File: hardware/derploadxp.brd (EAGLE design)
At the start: 59.1 x 61 mm, 53 parts, among them IC3 TC7660SO-08, J1 AVR_SPI_PRG_6NS, J2 POWER_JACKPTH, U1 ATMEGA328P_PDIP

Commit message: Resolved Issue #1 and #2 moved items around to add project name and version to top layer silkscreen
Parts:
- moved Y1 7.67 mm to (40.0, 32.4)
- moved C13 5.75 mm to (50.2, 36.8), turned to 270 degrees
- moved C14 5.68 mm to (45.7, 37.5)
- moved C1 4.58 mm to (48.3, 36.8), turned to 270 degrees
- moved C12 3.17 mm to (34.3, 36.8)
- moved C15 3.17 mm to (39.4, 36.8)
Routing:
- net PB7: track 22.8 -> 13.1 mm
- net PB6: track 17.4 -> 7.73 mm
- net 5V: track 155.4 -> 164.1 mm
- net N$11: track 27.2 -> 20.0 mm
- net GND: track 134.9 -> 133.0 mm
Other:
- board text added: "Derpload"
- board text added: "v1.0.0"

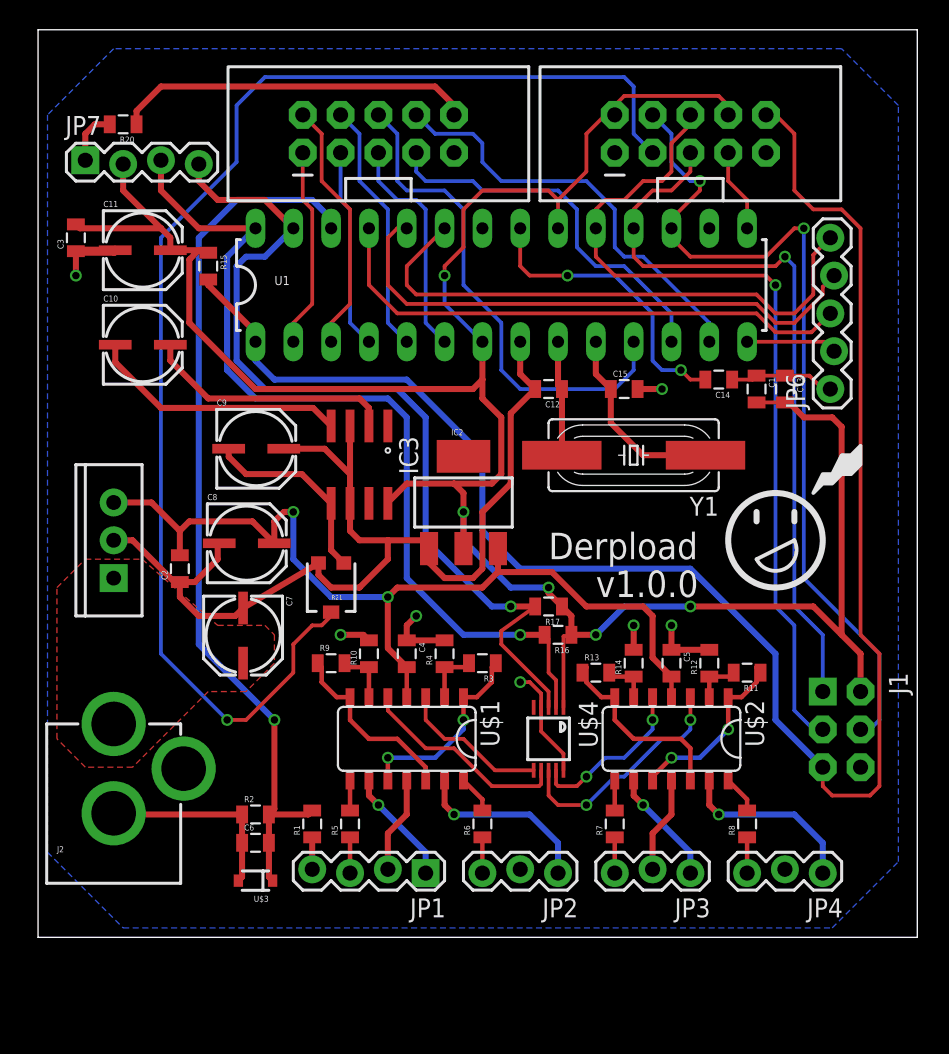
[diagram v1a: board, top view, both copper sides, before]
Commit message: Added one of two mounting holes to resolve Issue #3
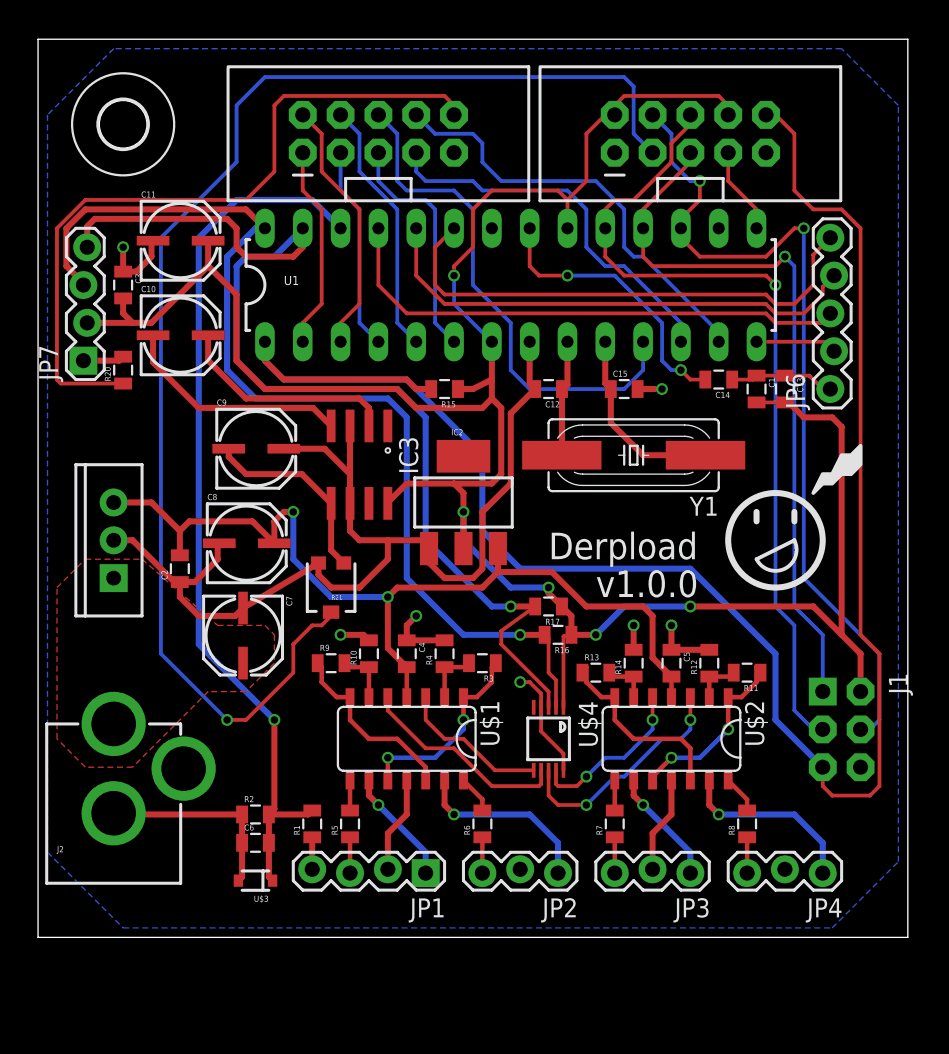
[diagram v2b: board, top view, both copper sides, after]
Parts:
- added U$7: (no value), holes:3,2
- moved R15 17.9 mm to (27.3, 36.8), turned to 180 degrees
- moved R20 16.5 mm to (5.71, 38.1), turned to 90 degrees
- moved JP7 13.3 mm to (3.17, 38.7), turned to 90 degrees
- moved C3 4.49 mm to (5.71, 43.8), turned to 270 degrees
- moved C11 2.62 mm to (9.53, 47.0)
- moved C10 2.62 mm to (9.53, 40.6)
- moved U1 0.64 mm to (31.8, 43.8)
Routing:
- net LED-: track 24.1 -> 48.6 mm
- net SDA: track 61.0 -> 72.2 mm
- net SCL: track 60.0 -> 69.8 mm
- net RESET: track 117.1 -> 124.2 mm
- net ROTARYA: track 37.3 -> 33.6 mm
- net ROTARYB: track 37.8 -> 34.4 mm
- net N$4: track 17.4 -> 15.5 mm
- net N$2: track 16.9 -> 15.0 mm
- net CS2: track 58.0 -> 56.4 mm
- net CS1: track 50.3 -> 48.6 mm
- net 5V: track 164.1 -> 162.7 mm
- net SELECT: track 36.6 -> 35.5 mm
- net N$11: track 20.0 -> 19.0 mm
- net A0: track 57.6 -> 56.7 mm
- net DB4: track 15.3 -> 15.9 mm
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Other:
- board size 59.1 x 61 mm -> 58.4 x 60.3 mm

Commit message: Added two of two mounting holes to resolve Issue #3
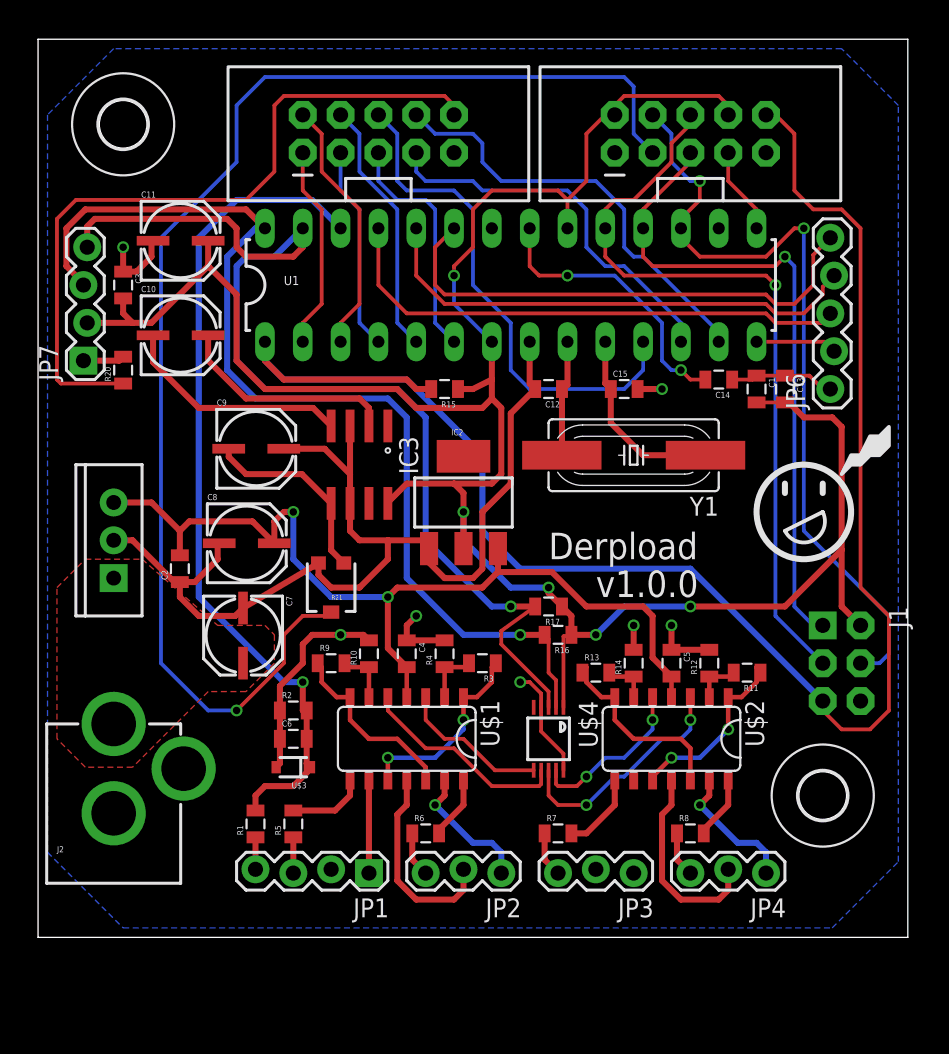
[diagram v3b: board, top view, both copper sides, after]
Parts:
- added U$5: (no value), holes:3,2
- moved U$3 8.03 mm to (17.1, 11.4)
- moved C6 7.43 mm to (17.1, 13.3)
- moved R2 7.43 mm to (17.1, 15.2)
- moved J1 4.44 mm to (54.0, 18.4)
- moved R7 3.86 mm to (34.9, 6.99), turned to 0 degrees
- moved R8 3.86 mm to (43.8, 6.99), turned to 0 degrees
- moved R6 3.86 mm to (26.0, 6.99), turned to 0 degrees
- moved JP1 3.81 mm to (22.2, 4.45)
- moved JP2 3.81 mm to (31.1, 4.45)
- moved R1 3.81 mm to (14.6, 7.62)
- moved R5 3.81 mm to (17.1, 7.62)
- moved JP3 3.81 mm to (40.0, 4.45)
- moved JP4 3.81 mm to (48.9, 4.45)
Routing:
- net GND: track 132.6 -> 145.5 mm
- net RESET: track 124.2 -> 115.4 mm
- net VSHUNT3: track 7.80 -> 0.00 mm, vias 1 -> 0
- net CS2: track 56.4 -> 51.6 mm
- net CS1: track 48.6 -> 44.5 mm
- net 5V: track 162.7 -> 159.0 mm
- net A0: track 56.7 -> 53.1 mm
- net N$10: track 2.02 -> 5.34 mm
- net VSENSE: track 59.9 -> 56.6 mm
- net VSHUNT2: track 12.3 -> 9.07 mm
- net VSHUNT4: track 12.3 -> 9.07 mm
- net N$3: track 2.02 -> 5.24 mm
- net N$8: track 2.54 -> 4.23 mm
- net N$9: track 2.54 -> 4.23 mm
- net VSHUNT1: track 7.80 -> 6.22 mm, vias 1 -> 0
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
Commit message: Added 12V aux port
Addresses issue #11
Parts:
- added JP5: (no value), SparkFun-Connectors:1X02_LOCK
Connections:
- net 12V: now also JP5.2
- net GND: now also JP5.1
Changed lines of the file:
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@@
 <?xml version="1.0" encoding="utf-8"?>
 <!DOCTYPE eagle SYSTEM "eagle.dtd">
-<eagle version="6.4">
+<eagle version="6.3">
 <drawing>
 <settings>
@@
 <layers>
 <layer number="1" name="Top" color="4" fill="1" visible="yes" active="yes"/>
+<layer number="2" name="Route2" color="1" fill="3" visible="no" active="no"/>
+<layer number="3" name="Route3" color="4" fill="3" visible="no" active="no"/>
+<layer number="4" name="Route4" color="1" fill="4" visible="no" active="no"/>
+<layer number="5" name="Route5" color="4" fill="4" visible="no" active="no"/>
+<layer number="6" name="Route6" color="1" fill="8" visible="no" active="no"/>
+<layer number="7" name="Route7" color="4" fill="8" visible="no" active="no"/>
+<layer number="8" name="Route8" color="1" fill="2" visible="no" active="no"/>
+<layer number="9" name="Route9" color="4" fill="2" visible="no" active="no"/>
+<layer number="10" name="Route10" color="1" fill="7" visible="no" active="no"/>
+<layer number="11" name="Route11" color="4" fill="7" visible="no" active="no"/>
+<layer number="12" name="Route12" color="1" fill="5" visible="no" active="no"/>
+<layer number="13" name="Route13" color="4" fill="5" visible="no" active="no"/>
+<layer number="14" name="Route14" color="1" fill="6" visible="no" active="no"/>
+<layer number="15" name="Route15" color="4" fill="6" visible="no" active="no"/>
 <layer number="16" name="Bottom" color="1" fill="1" visible="yes" active="yes"/>
 <layer number="17" name="Pads" color="2" fill="1" visible="yes" active="yes"/>
@@
 <element name="U$7" library="holes" package="3,2" value="" x="5.715" y="54.61"/>
 <element name="U$5" library="holes" package="3,2" value="" x="52.705" y="9.525"/>
+<element name="JP5" library="SparkFun-Connectors" package="1X02_LOCK" value="" x="1.905" y="-4.445"/>
 </elements>
 <signals>
@@
 <wire x1="17.78" y1="19.685" x2="18.415" y2="20.32" width="0.4064" layer="1"/>
 <wire x1="18.415" y1="20.32" x2="20.32" y2="20.32" width="0.4064" layer="1"/>
+<contactref element="JP5" pad="1"/>
+<wire x1="30.48" y1="47.625" x2="38.735" y2="52.705" width="0" layer="19" extent="1-1"/>
+<wire x1="33.02" y1="40.005" x2="30.48" y2="47.625" width="0" layer="19" extent="1-1"/>
+<wire x1="25.4" y1="21.59" x2="27.305" y2="24.13" width="0" layer="19" extent="1-1"/>
+<wire x1="22.225" y1="19.95" x2="24.765" y2="19.95" width="0" layer="19" extent="1-1"/>
+<wire x1="32.385" y1="17.145" x2="27.305" y2="19.95" width="0" layer="19" extent="1-1"/>
+<wire x1="40.27" y1="36.83" x2="33.39" y2="36.83" width="0" layer="19" extent="1-1"/>
+<wire x1="46.62" y1="37.465" x2="41.91" y2="36.83" width="0" layer="19" extent="1-1"/>
+<wire x1="40.005" y1="19.315" x2="33.79" y2="16.375" width="0" layer="19" extent="1-1"/>
+<wire x1="42.545" y1="20.955" x2="40.005" y2="20.955" width="0" layer="19" extent="1-1"/>
+<wire x1="37.465" y1="4.572" x2="35.29" y2="11.2219" width="0" layer="19" extent="1-1"/>
+<wire x1="41.91" y1="3.81" x2="37.465" y2="4.572" width="0" layer="19" extent="1-1"/>
+<wire x1="19.685" y1="4.572" x2="15.995" y2="11.43" width="0" layer="19" extent="1-1"/>
+<wire x1="24.13" y1="3.81" x2="19.685" y2="4.572" width="0" layer="19" extent="1-1"/>
+<wire x1="55.245" y1="15.875" x2="45.085" y2="19.315" width="0" layer="19" extent="1-1"/>
+<wire x1="5.08" y1="8.335" x2="15.995" y2="11.43" width="0" layer="19" extent="1-1"/>
+<wire x1="5.45" y1="38.735" x2="5.08" y2="26.67" width="0" layer="19" extent="1-1"/>
+<wire x1="5.715" y1="44.715" x2="5.715" y2="39" width="0" layer="19" extent="1-1"/>
+<wire x1="1.7272" y1="-4.445" x2="5.08" y2="8.335" width="0" layer="19" extent="1-1"/>
 </signal>
 <signal name="VSENSE">
@@
 <wire x1="10.16" y1="27.94" x2="14.4" y2="27.94" width="0.4064" layer="1"/>
 <wire x1="14.4" y1="27.94" x2="15.87" y2="26.47" width="0.4064" layer="1"/>
+<contactref element="JP5" pad="2"/>
+<wire x1="4.6228" y1="-4.445" x2="24.765" y2="16.135" width="0" layer="19" extent="1-1"/>
 </signal>
 <signal name="N$5">

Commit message: Added PDF and placed fan port on Board
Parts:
- moved JP5 38.8 mm to (3.81, 34.3)
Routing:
- net 12V: track 62.2 -> 67.9 mm
- net GND: track 145.5 -> 150.9 mm
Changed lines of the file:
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@@
 <element name="U$7" library="holes" package="3,2" value="" x="5.715" y="54.61"/>
 <element name="U$5" library="holes" package="3,2" value="" x="52.705" y="9.525"/>
-<element name="JP5" library="SparkFun-Connectors" package="1X02_LOCK" value="" x="1.905" y="-4.445"/>
+<element name="JP5" library="SparkFun-Connectors" package="1X02_LOCK" value="" x="3.81" y="34.29"/>
 </elements>
 <signals>
@@
 <wire x1="7.62" y1="45.72" x2="7.62" y2="46.685" width="0.4064" layer="1"/>
 <wire x1="7.62" y1="46.685" x2="7.725" y2="46.79" width="0.4064" layer="1"/>
-<wire x1="3.048" y1="38.735" x2="5.45" y2="38.735" width="0.4064" layer="1"/>
-<wire x1="5.45" y1="38.735" x2="5.715" y2="39" width="0.4064" layer="1"/>
 <via x="5.715" y="46.355" extent="1-16" drill="0.5"/>
 <wire x1="5.715" y1="44.715" x2="5.715" y2="46.355" width="0.4064" layer="1"/>
@@
 <wire x1="37.465" y1="4.572" x2="35.29" y2="11.2219" width="0" layer="19" extent="1-1"/>
 <wire x1="41.91" y1="3.81" x2="37.465" y2="4.572" width="0" layer="19" extent="1-1"/>
+<wire x1="3.048" y1="38.735" x2="3.6322" y2="34.29" width="0" layer="19" extent="1-1"/>
+<wire x1="5.715" y1="39" x2="3.048" y2="38.735" width="0" layer="19" extent="1-1"/>
+<wire x1="5.715" y1="44.715" x2="5.715" y2="39" width="0" layer="19" extent="1-1"/>
 <wire x1="19.685" y1="4.572" x2="15.995" y2="11.43" width="0" layer="19" extent="1-1"/>
 <wire x1="24.13" y1="3.81" x2="19.685" y2="4.572" width="0" layer="19" extent="1-1"/>
 <wire x1="55.245" y1="15.875" x2="45.085" y2="19.315" width="0" layer="19" extent="1-1"/>
 <wire x1="5.08" y1="8.335" x2="15.995" y2="11.43" width="0" layer="19" extent="1-1"/>
-<wire x1="5.45" y1="38.735" x2="5.08" y2="26.67" width="0" layer="19" extent="1-1"/>
-<wire x1="5.715" y1="44.715" x2="5.715" y2="39" width="0" layer="19" extent="1-1"/>
-<wire x1="1.7272" y1="-4.445" x2="5.08" y2="8.335" width="0" layer="19" extent="1-1"/>
+<wire x1="3.6322" y1="34.29" x2="3.6322" y2="28.1178" width="0.4064" layer="16"/>
+<wire x1="3.6322" y1="28.1178" x2="5.08" y2="26.67" width="0.4064" layer="16"/>
 </signal>
 <signal name="VSENSE">
@@
 <wire x1="14.4" y1="27.94" x2="15.87" y2="26.47" width="0.4064" layer="1"/>
 <contactref element="JP5" pad="2"/>
-<wire x1="4.6228" y1="-4.445" x2="24.765" y2="16.135" width="0" layer="19" extent="1-1"/>
+<wire x1="6.5278" y1="34.29" x2="6.5278" y2="30.6578" width="0.4064" layer="16"/>
+<wire x1="6.5278" y1="30.6578" x2="5.08" y2="29.21" width="0.4064" layer="16"/>
 </signal>
 <signal name="N$5">

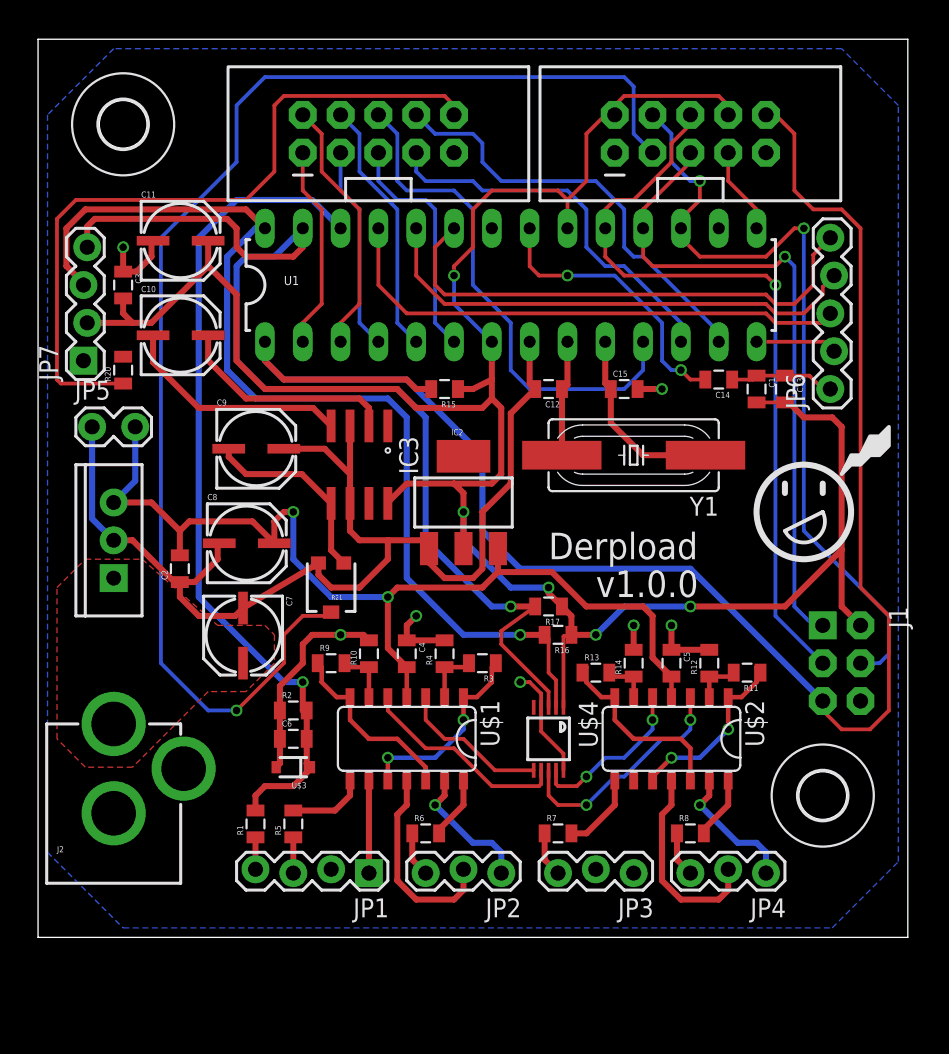
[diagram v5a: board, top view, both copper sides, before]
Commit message: rearranged and corrected visible silkscreen for component values and names to solve Issue #8
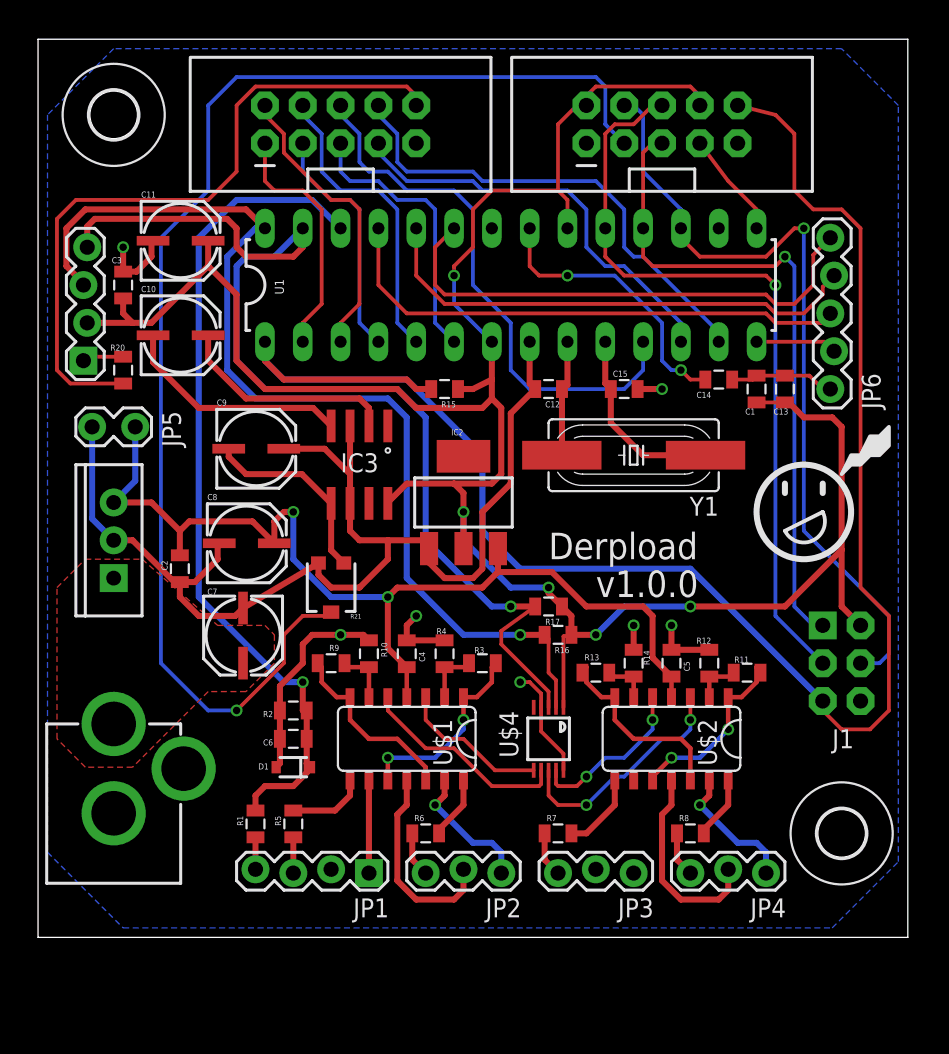
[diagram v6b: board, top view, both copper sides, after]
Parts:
- J1: value AVR_SPI_PRG_6NS -> SPI
- moved U$5 2.84 mm to (54.0, 6.99)
- moved LCD2 2.62 mm to (20.3, 54.6)
- moved LCD1 2.01 mm to (41.9, 54.6)
- moved U$7 0.90 mm to (5.08, 55.2)
- renumbered U$3 to D1
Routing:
- net DB7: track 29.2 -> 32.8 mm
- net DB3: track 17.3 -> 20.5 mm
- net DB0: track 13.8 -> 16.6 mm
- net DB4: track 15.9 -> 18.7 mm
- net GND: track 150.9 -> 153.7 mm
- net LED-: track 48.9 -> 46.3 mm
- net DB6: track 26.0 -> 28.4 mm
- net DB1: track 17.3 -> 19.8 mm
- net DB2: track 13.8 -> 16.2 mm
- net DB5: track 34.5 -> 37.0 mm
- net RESET: track 115.4 -> 117.4 mm
- net VO: track 89.0 -> 87.6 mm
- net CLK: track 5.87 -> 7.14 mm
- net 5V: track 159.0 -> 158.5 mm
- net A0: track 53.1 -> 53.5 mm, vias 2 -> 1
